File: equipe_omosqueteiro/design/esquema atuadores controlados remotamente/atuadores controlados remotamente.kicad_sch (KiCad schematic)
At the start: 20 parts, among them J1 Screw_Terminal_01x02, J2 Conn_01x04_Socket, M1 Motor_Servo, M2 Motor_Servo, M3 Motor_Servo, M4 Motor_Servo, M5 Motor_Servo, U3 StepDown_LM2596HV, U4 LM1117T-3.3

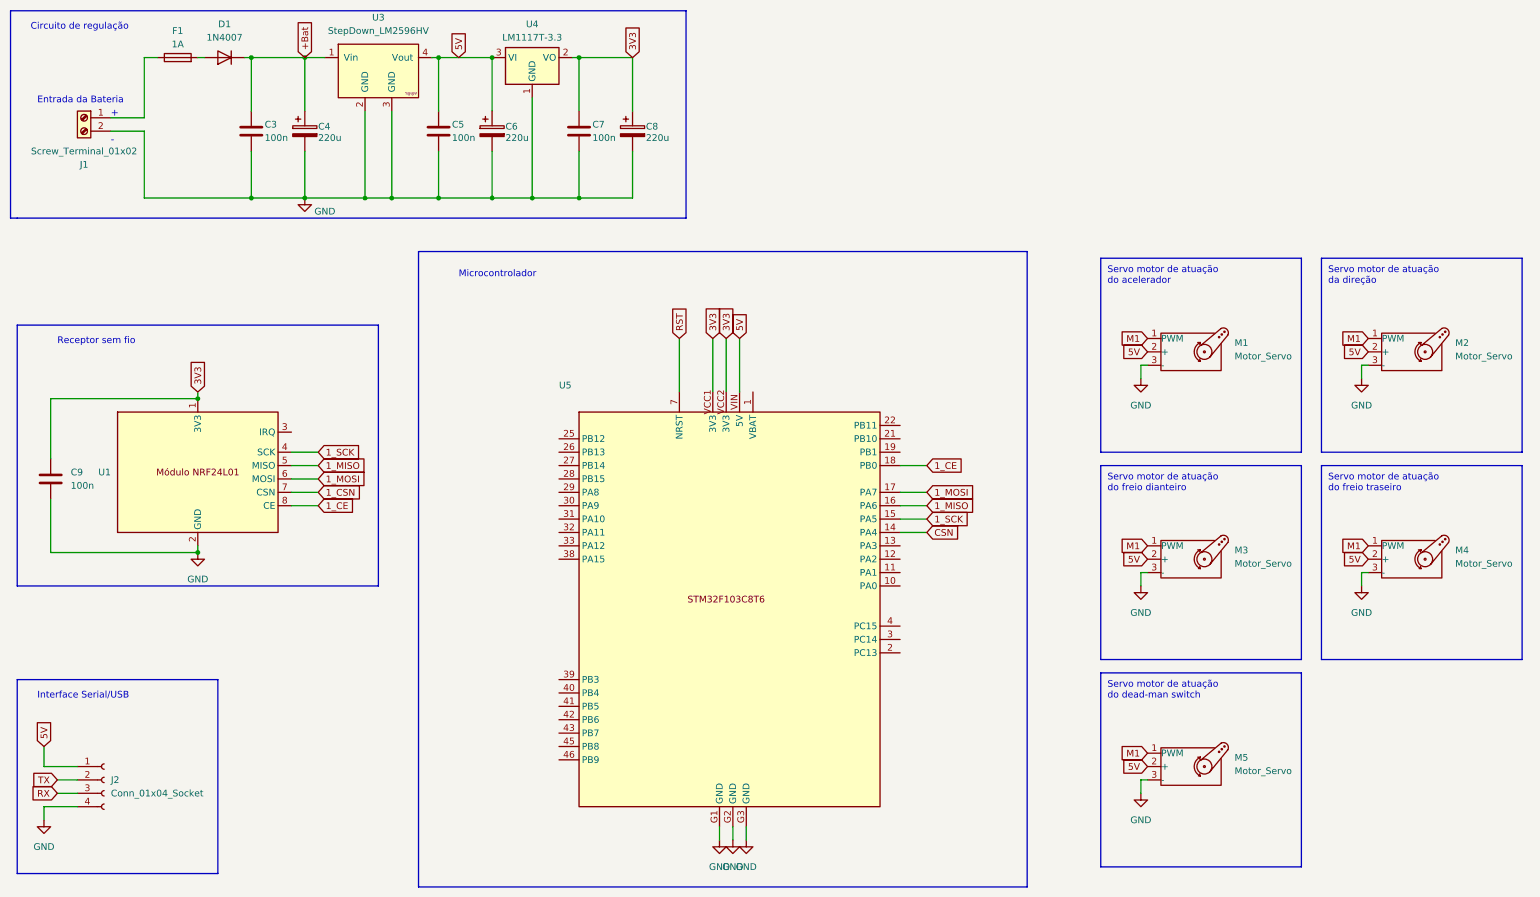
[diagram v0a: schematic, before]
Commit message: adicionado diagramas e texto design
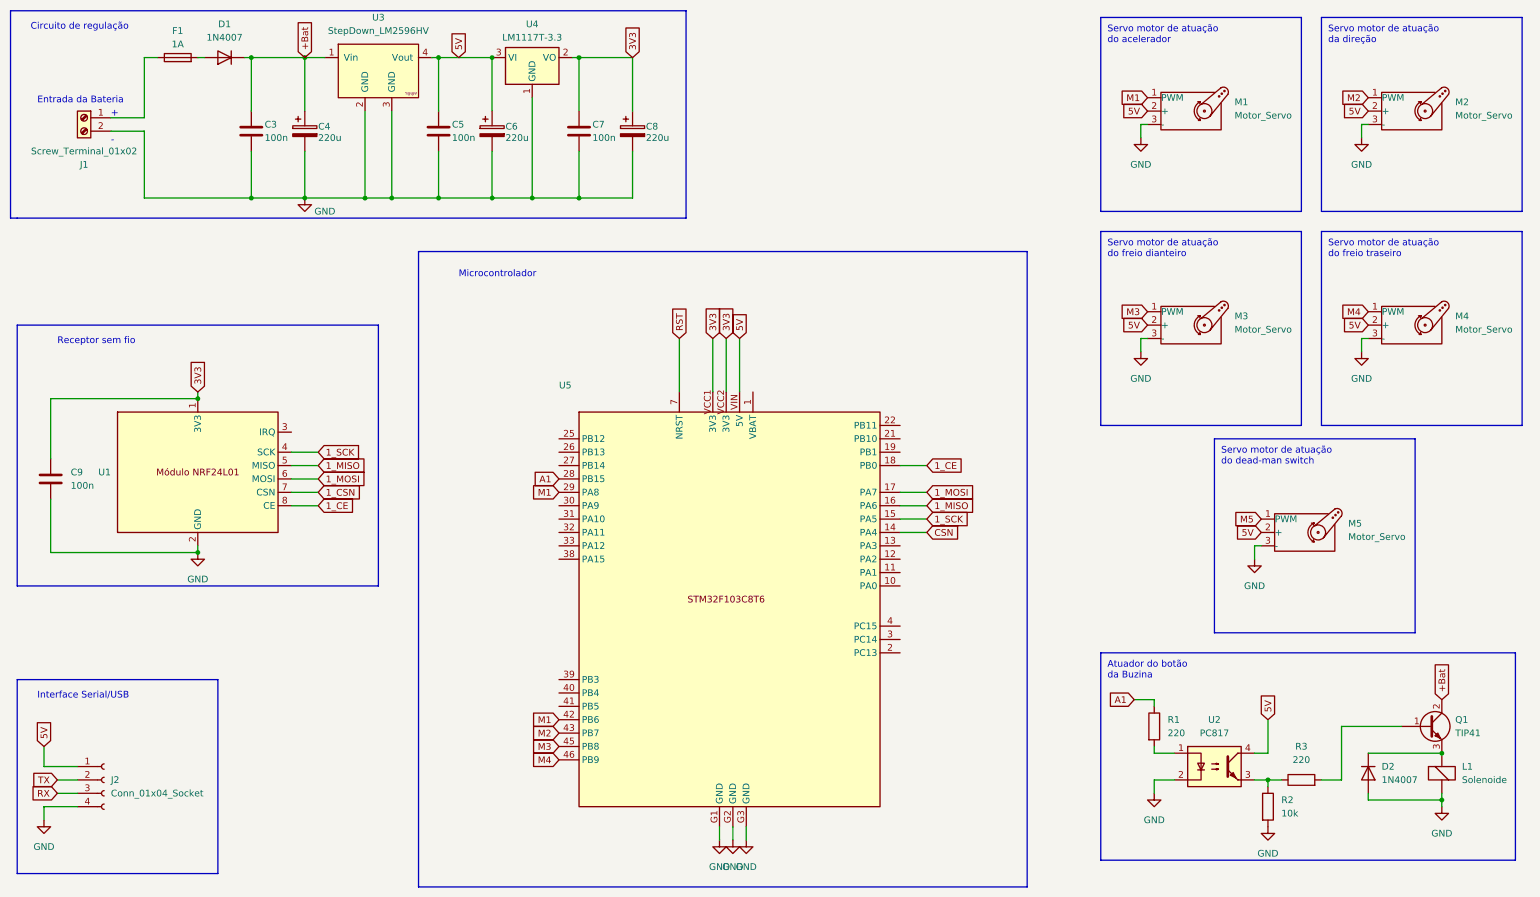
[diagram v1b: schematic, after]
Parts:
- added D2: 1N4007, Diode_THT:D_DO-41_SOD81_P10.16mm_Horizontal, symbol Diode:1N4007
- added L1: Solenoide, symbol Device:ElectromagneticActor
- added Q1: TIP41, Package_TO_SOT_THT:TO-220-3_Vertical, symbol Transistor_BJT:TIP41
- added R1, R3: 220, symbol Device:R
- added R2: 10k, symbol Device:R
- added U2: PC817, Package_DIP:DIP-4_W7.62mm, symbol Isolator:PC817
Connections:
- net +Bat: now also Q1.2 (C)
- net 5V: now also U2.4
- net GND: now also D2.2 (A), L1.2 (+), R2.2, U2.2
- net M1: now also U5.29 (PA8), U5.42 (PB6); no longer M2.1 (PWM), M3.1 (PWM), M4.1 (PWM), M5.1 (PWM)
- net A1: now reaches U5.28 (PB15)
- net A1: now also R1.1
- net M2: now reaches U5.43 (PB7)
- net M2: now also M2.1 (PWM)
- net M3: now reaches U5.45 (PB8)
- net M3: now also M3.1 (PWM)
- net M4: now reaches U5.46 (PB9)
- net M4: now also M4.1 (PWM)
- new net: D2.1 (K), L1.1 (-), Q1.3 (E)
- new net: R1.2, U2.1
- new net: R2.1, R3.1, U2.3
- new net: Q1.1 (B), R3.2
- new net M5: M5.1 (PWM)
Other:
- note added: "Atuador do botão da Buzina"
- moved on the sheet: M1, M2, M3, M4, M5
